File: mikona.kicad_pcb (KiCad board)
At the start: 4 copper layers, 50 x 40 mm, 79 parts, among them J1 TC2030-IDC-NL, Q1 BSC109N10NS3G, Q2 STN3N40K3, Q3 IGB50N60T, Q4 IGB50N60T, U1 LT3750EMSTR, U10 MX25V1006FZUI, U11 MIC5528-3.3, U2 ZXGD3009E6, U3 NCS325, U4 STM32F042G6Ux, U5 IX4427MTR, U6 KTD2026EWE-TR, U7 ATA6561-GBQW, U8 AP63205WU, U9 MCP4562T-503E

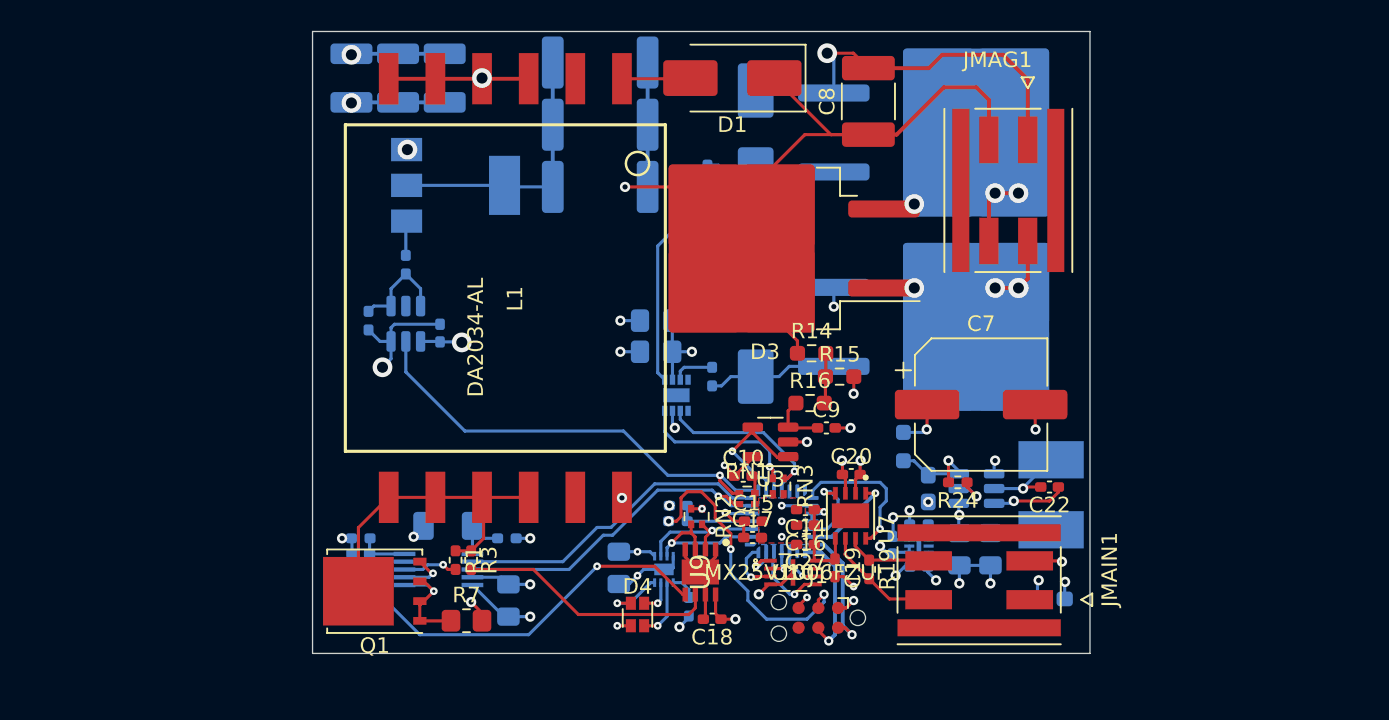
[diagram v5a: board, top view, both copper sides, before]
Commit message: Add jlpcb rules and fix many violations.
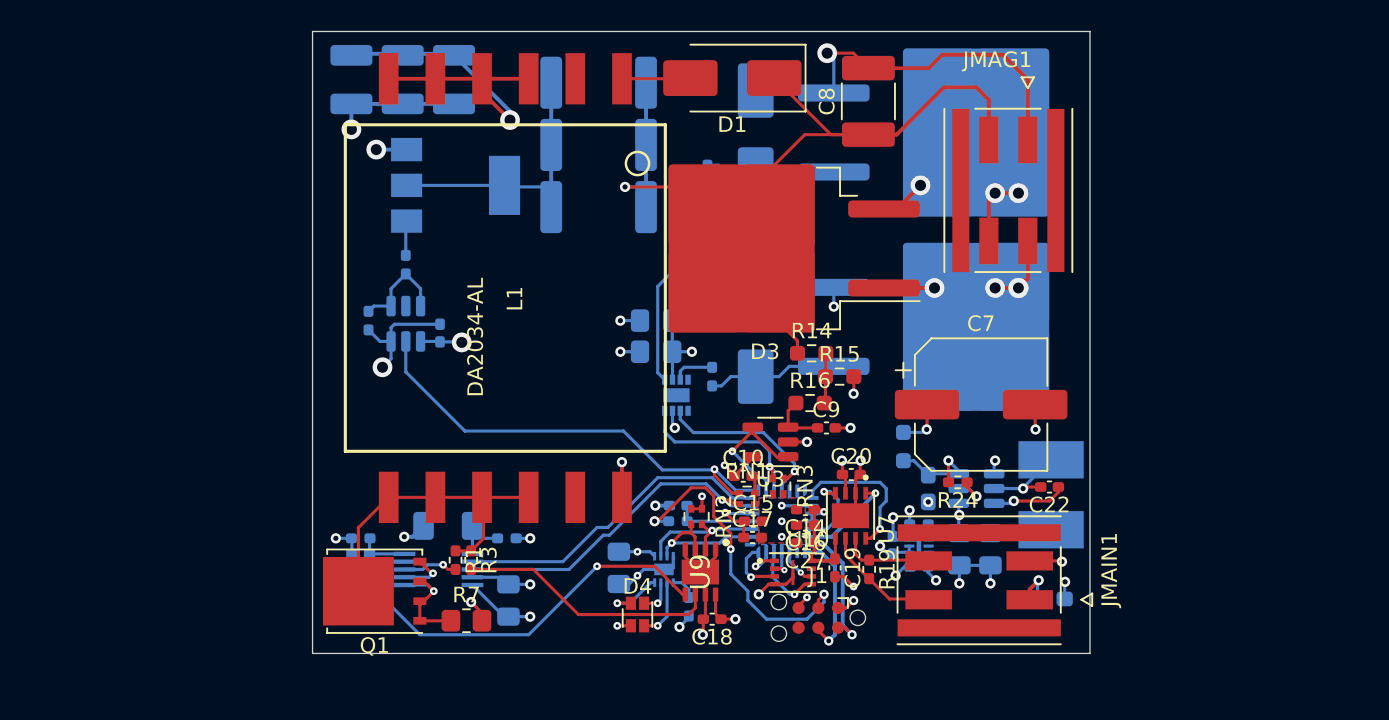
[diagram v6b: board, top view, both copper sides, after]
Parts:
- U10: footprint MX25V1006FZUI:MX25V1006FZUI -> MX25V1006FZUI:PSON50P200X300X60-9N
- moved R10 1.30 mm to (141.9, 92.3)
- moved R11 1.30 mm to (141.9, 96.3)
- moved R9 1.30 mm to (141.9, 88.3)
- moved C5 0.61 mm to (132.6, 88.1)
- moved C6 0.32 mm to (129.3, 88.1)
- moved C27 0.10 mm to (155.2, 117.9)
- moved C4 0.10 mm to (126.0, 88.1)
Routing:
- net GND: track 98.1 -> 111.0 mm, vias 33 -> 34
- net +24V: track 31.9 -> 40.9 mm, vias 8 -> 7
- net /MAGNET_A_2: track 4.77 -> 8.02 mm
- net /MAGNET_B_2: track 4.74 -> 7.72 mm
- net /Logic/SW_NRST: track 19.2 -> 20.8 mm
- net Net-(F1-Pad1): track 1.23 -> 2.72 mm
- net VDC: track 57.9 -> 59.4 mm
- net +3.3V: track 22.0 -> 23.3 mm
- net /Logic/DISCHARGE: track 29.7 -> 30.3 mm

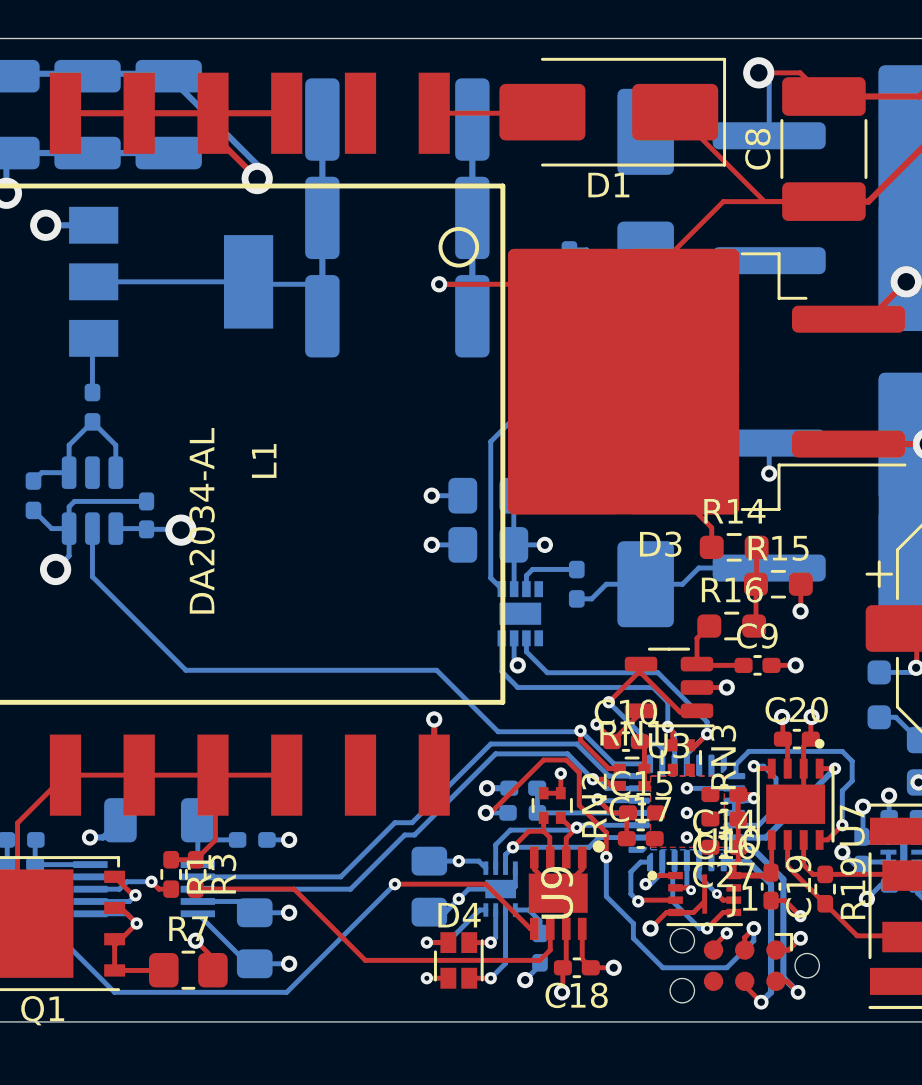
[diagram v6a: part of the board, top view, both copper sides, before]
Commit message: Move the flash mem to bottom layer, we're now error-free, yay :D
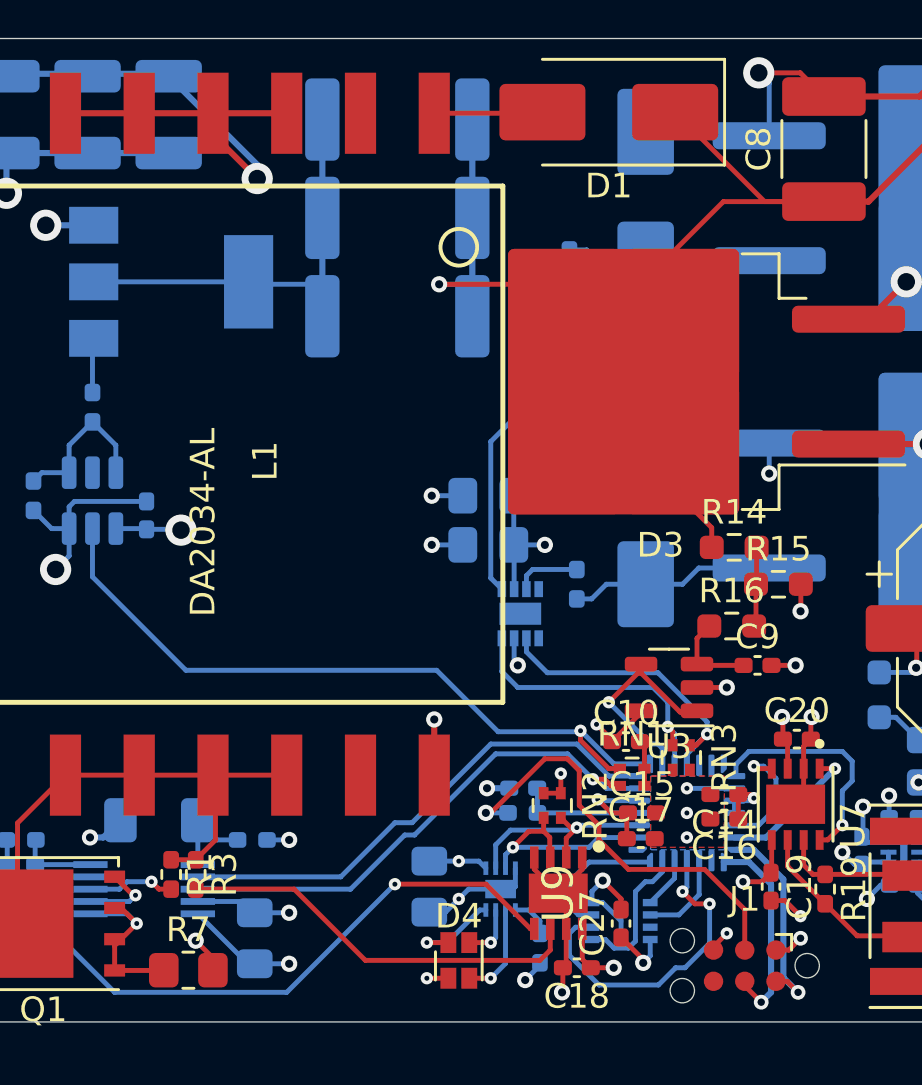
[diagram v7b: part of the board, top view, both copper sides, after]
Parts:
- U10: moved to B.Cu
- moved C27 5.22 mm to (151.0, 121.0), turned to 90 degrees
- moved U10 3.57 mm to (151.0, 120.9)
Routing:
- net /Logic/MISO: track 1.98 -> 13.1 mm, vias 1 -> 2
- net /Logic/FLASH_CS: track 2.72 -> 5.93 mm, vias 1 -> 0
- net /Logic/SW_NRST: track 20.8 -> 17.7 mm, vias 3 -> 1
- net /Logic/MOSI: track 4.90 -> 2.12 mm, vias 1 -> 0
- net /Logic/FLASH_WP: track 3.80 -> 5.58 mm, vias 1 -> 0
- net /Logic/SCK: track 2.45 -> 3.72 mm, vias 1 -> 0
- net GND: track 111.0 -> 111.9 mm
- net +3.3V: track 23.3 -> 22.9 mm, vias 7 -> 9

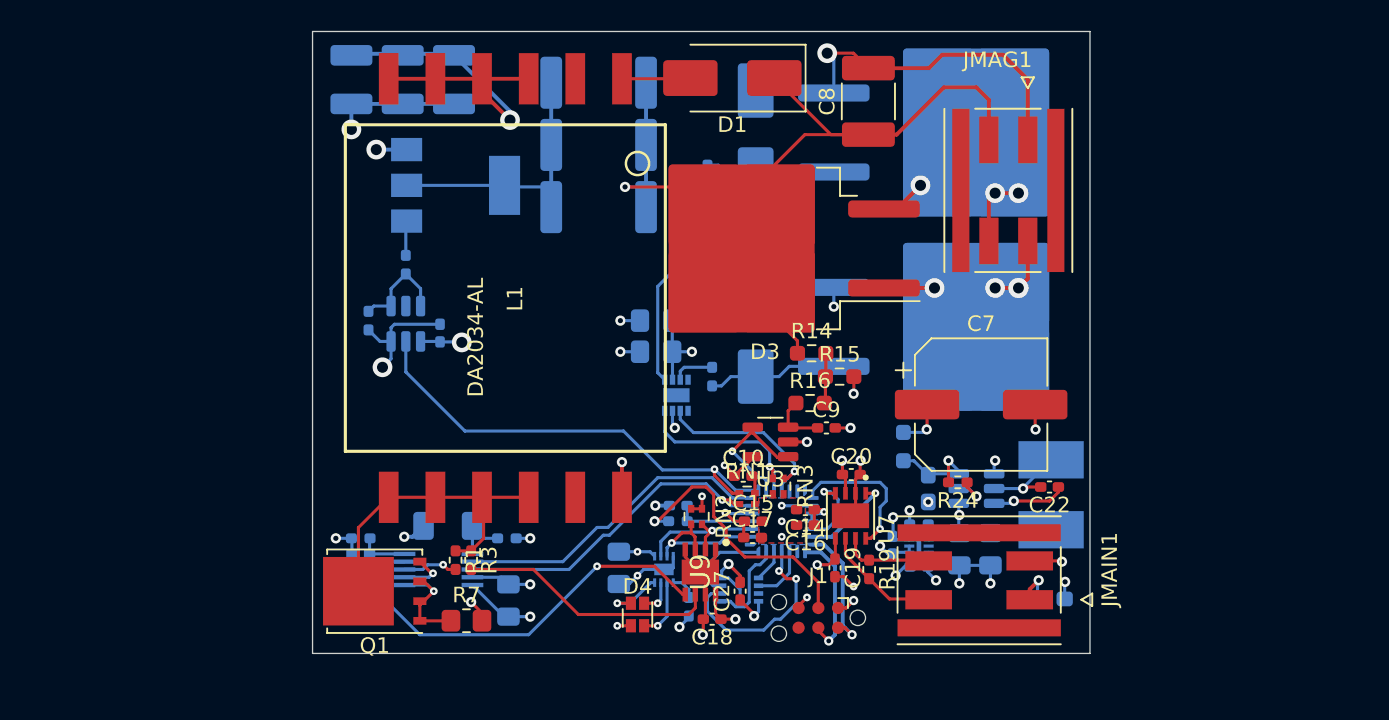
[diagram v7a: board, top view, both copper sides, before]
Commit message: Improve routing, almost there.
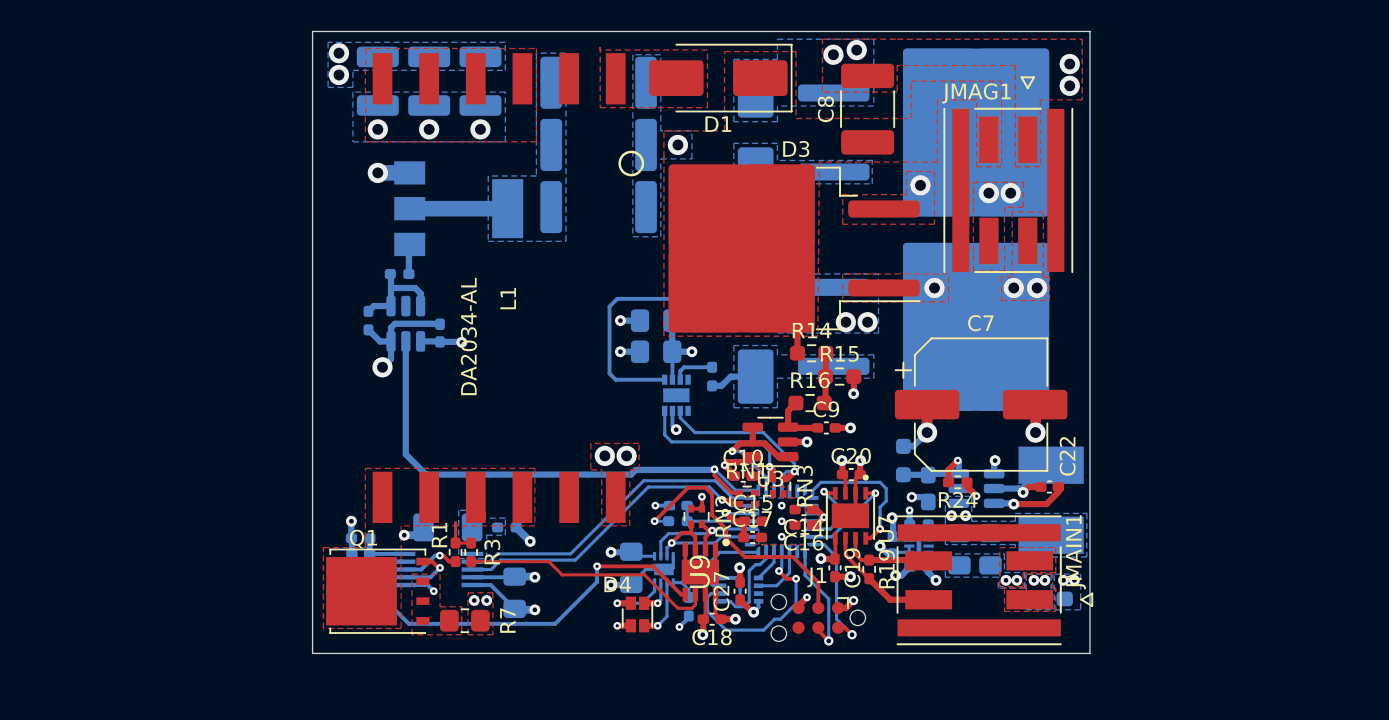
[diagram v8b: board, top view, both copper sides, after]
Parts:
- moved C4 8.30 mm to (134.3, 88.2), turned to -90 degrees
- moved C5 4.90 mm to (127.7, 88.2), turned to -90 degrees
- moved C6 1.70 mm to (131.0, 88.2), turned to -90 degrees
- moved Q2 1.51 mm to (132.9, 96.4)
- moved D1 0.90 mm to (149.6, 88.0)
- moved FB2 0.90 mm to (161.5, 112.6)
- moved C12 0.80 mm to (144.0, 119.5)
- moved R8 0.72 mm to (129.1, 100.6), turned to 180 degrees
- moved R5 0.70 mm to (136.0, 116.9)
- moved C1 0.64 mm to (136.5, 121.1)
- moved R17 0.63 mm to (149.1, 94.8)
- moved R1 0.50 mm to (132.7, 118.5)
- moved R3 0.50 mm to (133.7, 118.5)
- moved C8 0.50 mm to (159.2, 90.0)
- moved L1 0.40 mm to (135.5, 101.5)
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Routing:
- net GND: track 111.9 -> 58.3 mm, vias 34 -> 40
- net VDC: track 59.4 -> 12.7 mm
- net +24V: track 40.9 -> 17.2 mm, vias 7 -> 10
- net /Power/NMOS_DRAIN: track 20.7 -> 2.44 mm
- net Net-(Q2-D-Pad2): track 17.4 -> 6.44 mm
- net /MAGNET_A_2: track 8.02 -> 0.00 mm
- net /MAGNET_B_2: track 7.72 -> 0.00 mm
- net +5V: track 17.3 -> 9.90 mm, vias 7 -> 8
- net Net-(U5-OUT_B): track 14.1 -> 21.0 mm
- net Net-(D5-A1): track 8.44 -> 2.90 mm
- net Net-(D2-A1): track 8.35 -> 3.05 mm
- net Net-(U1-SOURCE): track 7.49 -> 2.33 mm
- net Net-(D1-A): track 4.42 -> 0.06 mm
- net Net-(U1-VTRANS): track 3.78 -> 0.00 mm
- net /Logic/DISCHARGE: track 30.3 -> 33.6 mm
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- added copper zone on B.Cu, net +24V
- added copper zone on F.Cu, net +24V
- added copper zone on B.Cu, net +5V
- added copper zone on F.Cu, net /MAGNET_A_2
- added copper zone on F.Cu, net /MAGNET_B_2
- added copper zone on F.Cu, net /Power/NMOS_DRAIN
- added copper zone on F.Cu, net Net-(D1-A)
- added copper zone on B.Cu, net Net-(D2-A1)
- added copper zone on B.Cu, net Net-(D5-A1)
- added copper zone on B.Cu, net Net-(F1-Pad1)
- added copper zone on F.Cu, net Net-(F1-Pad1)
- added copper zone on B.Cu, net Net-(Q2-D-Pad2)
- added copper zone on F.Cu, net Net-(U1-SOURCE)
- added copper zone on B.Cu, net Net-(U1-VTRANS)
- added copper zone on B.Cu, net VDC
- added copper zone on F.Cu, net VDC
